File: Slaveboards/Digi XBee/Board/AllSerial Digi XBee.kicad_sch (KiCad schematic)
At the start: 2 parts, among them X1 AllSerial Slaveboard

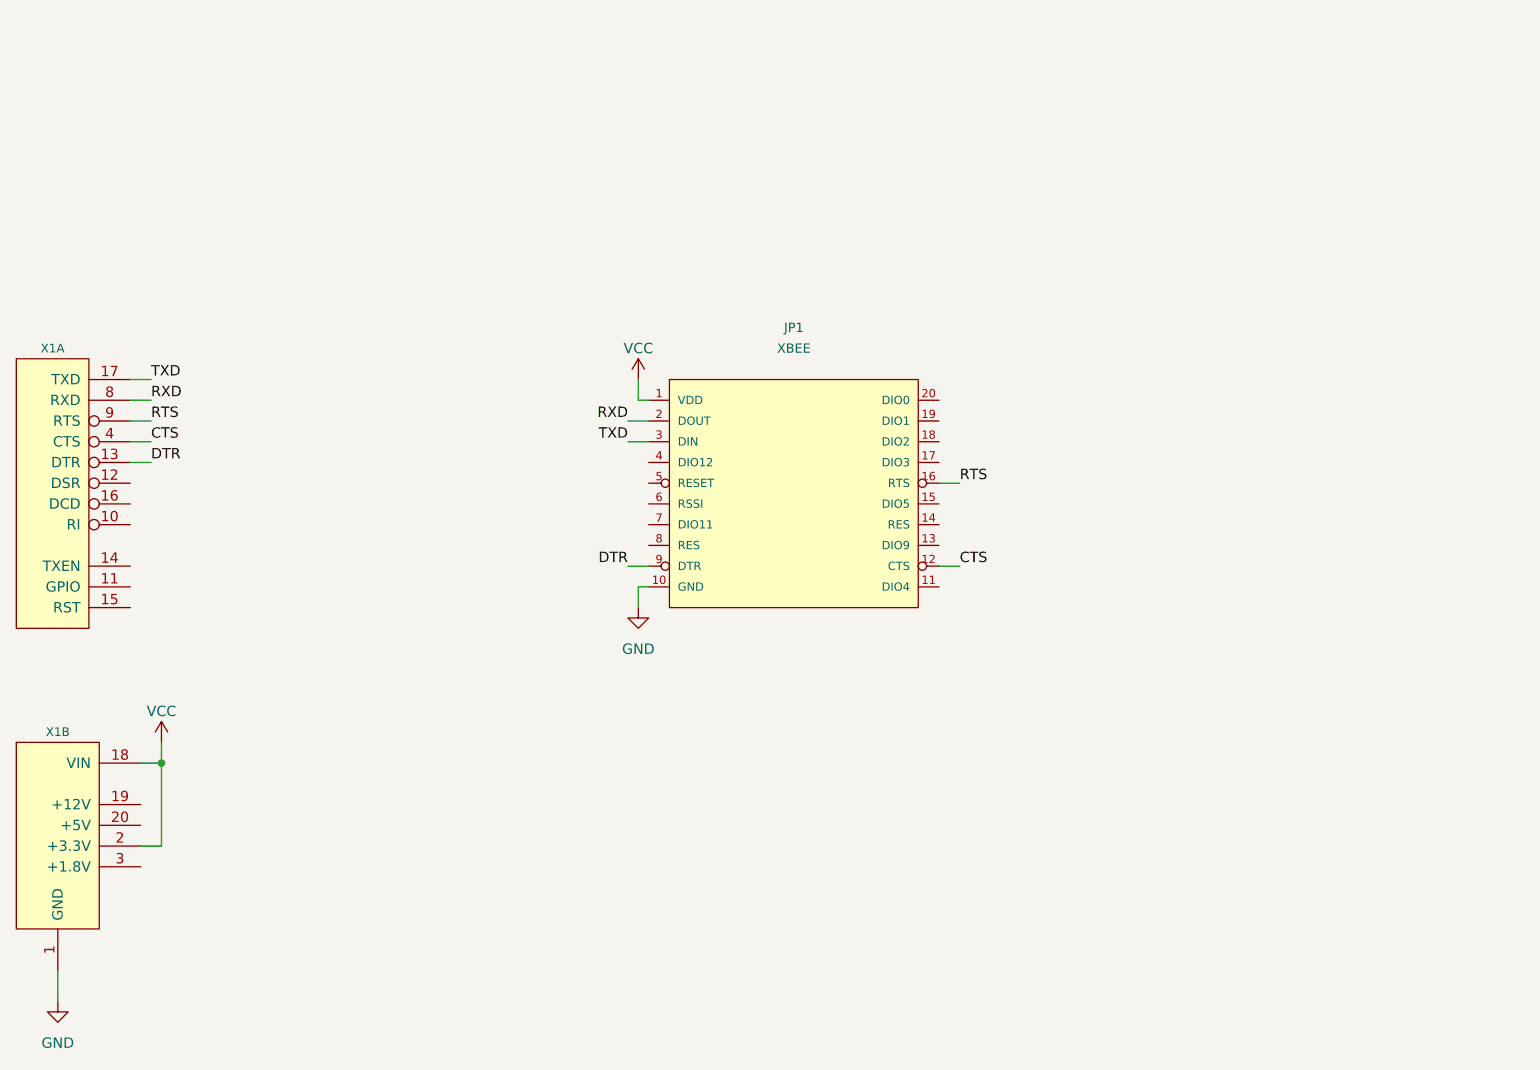
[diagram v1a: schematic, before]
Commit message: Migrate to KiCad 9
Add eBus board
Add various libraries
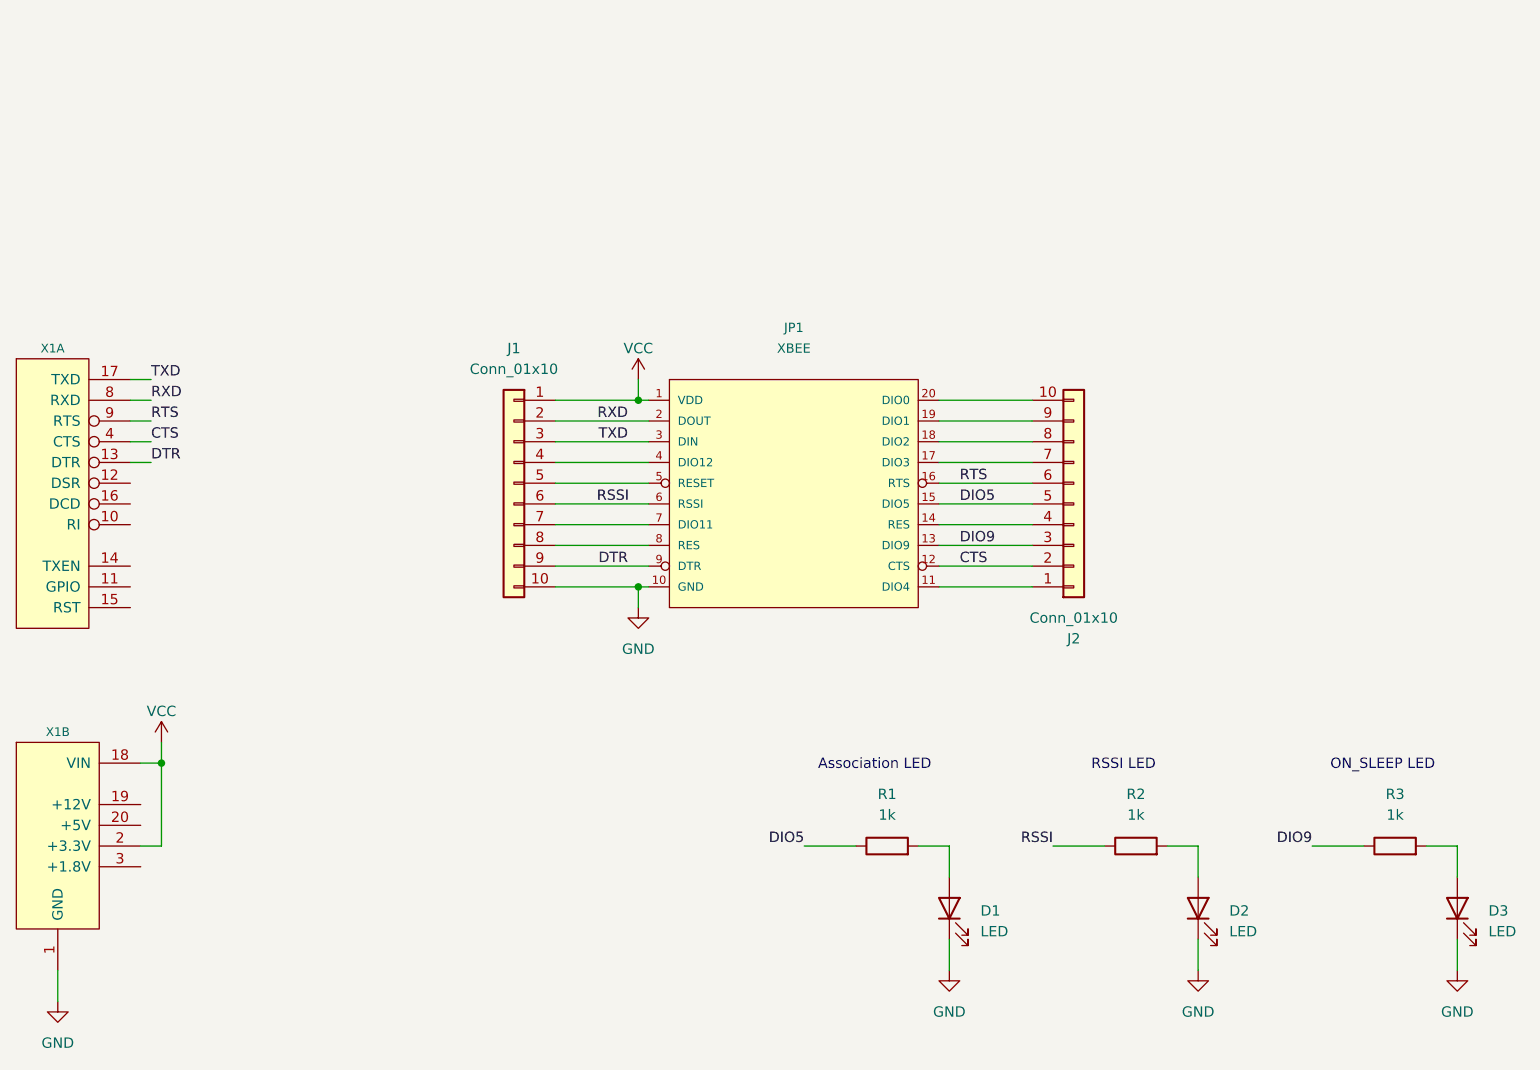
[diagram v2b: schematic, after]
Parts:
- added D1, D2, D3: LED, LED_SMD:LED_0805_2012Metric, symbol Device:LED
- added J1, J2: Conn_01x10, Connector_PinHeader_2.54mm:PinHeader_1x10_P2.54mm_Vertical, symbol Connector_Generic:Conn_01x10
- added R1, R2, R3: 1k, Resistor_SMD:R_0805_2012Metric, symbol Device:R
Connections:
- net CTS: now also J2.2 (Pin_2)
- net DTR: now also J1.9 (Pin_9)
- net GND: now also D1.1 (K), D2.1 (K), D3.1 (K), J1.10 (Pin_10)
- net RTS: now also J2.6 (Pin_6)
- net RXD: now also J1.2 (Pin_2)
- net TXD: now also J1.3 (Pin_3)
- net VCC: now also J1.1 (Pin_1)
- net at JP1.11 (DIO4): now also J2.1 (Pin_1)
- net DIO9: now reaches JP1.13 (DIO9)
- net DIO9: now also J2.3 (Pin_3), R3.1
- net at JP1.14 (RES): now also J2.4 (Pin_4)
- net DIO5: now reaches JP1.15 (DIO5)
- net DIO5: now also J2.5 (Pin_5), R1.1
- net at JP1.17 (DIO3): now also J2.7 (Pin_7)
- net at JP1.18 (DIO2): now also J2.8 (Pin_8)
- net at JP1.19 (DIO1): now also J2.9 (Pin_9)
- net at JP1.20 (DIO0): now also J2.10 (Pin_10)
- net at JP1.4 (DIO12): now also J1.4 (Pin_4)
- net at JP1.5 (RESET): now also J1.5 (Pin_5)
- net RSSI: now reaches JP1.6 (RSSI)
- net RSSI: now also J1.6 (Pin_6), R2.1
- net at JP1.7 (DIO11): now also J1.7 (Pin_7)
- net at JP1.8 (RES): now also J1.8 (Pin_8)
- new net: D3.2 (A), R3.2
- new net: D1.2 (A), R1.2
- new net: D2.2 (A), R2.2
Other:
- note added: "Association LED"
- note added: "ON_SLEEP LED"
- note added: "RSSI LED"

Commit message: Improve libraries
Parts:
- added D4: GN, LED_SMD:LED_0805_2012Metric, symbol Device:LED
- added J3: Conn_01x02, AllSerial:Metz_PT11302HBBN_182, symbol Connector_Generic:Conn_01x02
- added R4: 220, Resistor_SMD:R_0805_2012Metric, symbol Device:R
- added R5: 1k, Resistor_SMD:R_0805_2012Metric, symbol Device:R
- added S1, S2, S3: 31-XX, Button_Switch_SMD:SW_SPST_CK_RS282G05A3, symbol Switch:SW_Push
- D1: value LED -> YL
- D2: value LED -> RD
- D3: value LED -> GN
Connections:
- net GND: now also S1.2, S2.2, S3.2
- net DIO0: now reaches J2.10 (Pin_10), JP1.20 (DIO0)
- net DIO0: now also S1.1
- net RST: now reaches J1.7 (Pin_7), JP1.7 (DIO11)
- net RST: now also S3.1
- net VCC renamed +3.3V
- net +3.3V: now also R5.2
- new net: R4.1, S2.1
- new net: D4.2 (A), R5.1
- new net DIO4: D4.1 (K), R4.2
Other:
- note added: "Commissioning BTN"
- note added: "Reset BTN"
- note added: "User BTN/LED"
- moved on the sheet: J1, J2, JP1
